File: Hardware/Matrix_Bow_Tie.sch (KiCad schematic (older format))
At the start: 2 parts, among them U1 MAX4466

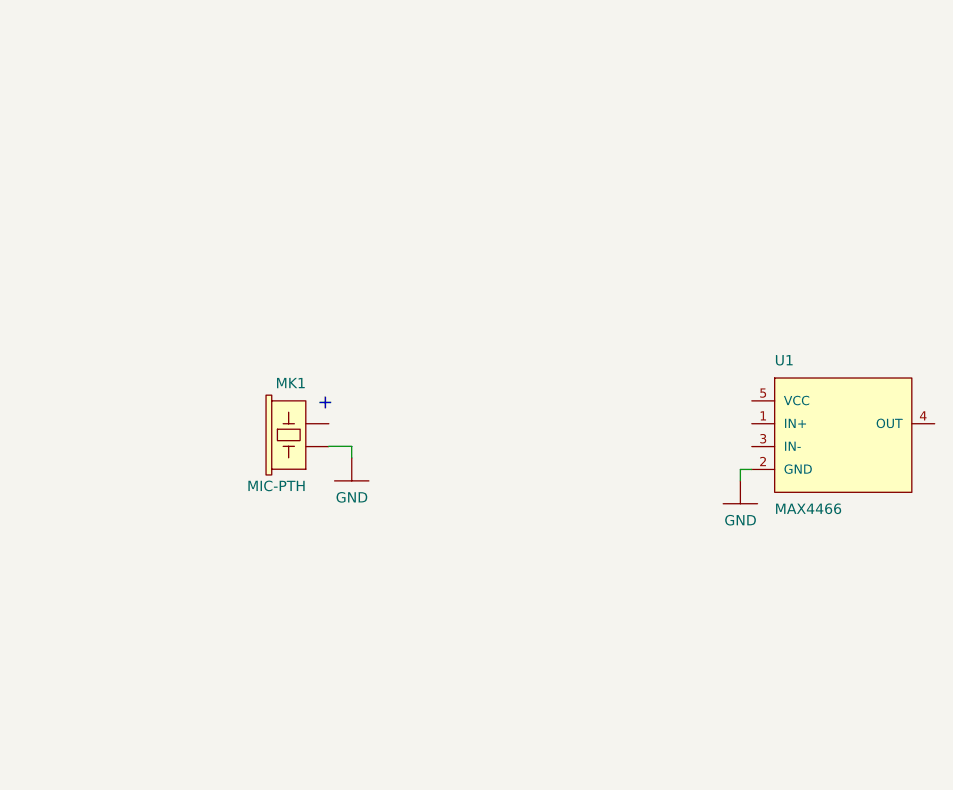
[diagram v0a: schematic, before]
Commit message: Added trimpot footprint and drew mic amp circuit.
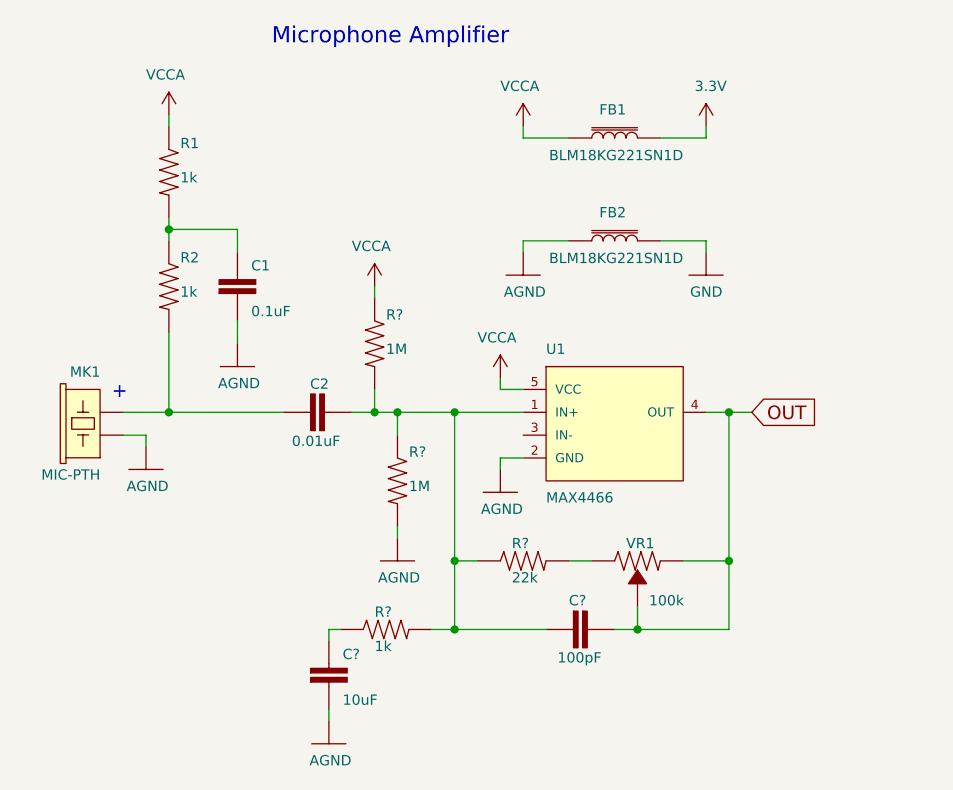
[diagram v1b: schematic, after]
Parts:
- added C1: 0.1uF, 0603, symbol 0.1UF-0603-25V-_+80_-20%_
- added C2: 0.01uF, 0603, symbol 0.1UF-0603-25V-_+80_-20%_
- added C?: 10uF, 0805, symbol 10UF-0805-10V-10%
- added C?: 100pF, 0603, symbol 100PF-0603-50V-5%
- added FB1, FB2: BLM18KG221SN1D, 0603, symbol FERRITE_BEAD-0603
- added R1, R2, R?: 1k, 0603, symbol 1KOHM-0603-1_10W-1%
- added R? (x2): 1M, 0603, symbol 1MOHM-0603-1_4W-5%
- added R?: 22k, 0603, symbol 22KOHM-0603-1_10W-1%
- added VR1: 100k, TC33X, symbol TRIMPOT-TC33X-2
- MK1: footprint Silicon-Custom:MICROPHONE-PTH-9.7MM -> MICROPHONE-PTH-9.7MM
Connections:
- net labels added: 3.3V, AGND, OUT, VCCA
- wire segments 4 -> 38
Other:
- note added: "Microphone Amplifier"
- moved on the sheet: U1

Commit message: Parts mostly laid out
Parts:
- added C5: 0.1uF, Capacitors:0603, symbol 0.1UF-0603-25V-_+80_-20%_
- added D1, D10, D11, D12, D13, D14, D15, D16, D17, D18, D19, D2, D20, D21, D22, D23, D24, D25, D26, D27, D28, D29, D3, D30, D31, D32, D33, D34, D35, D36, D37, D38, D39, D4, D40, D5, D6, D7, D8, D9: Yellow, LED:LED-0603, symbol LED0603
- added H1, H2: STAND-OFF, STAND-OFF, symbol STAND-OFF
- added J1, J2: CONN_12, Matrix_Bot_Tie:1X12_SMD_MALE, symbol CONN_12
- added Q1, Q2, Q3, Q4: TRANS_NPN_DUAL-MBT3904DW1T1, Silicon-Standard:SC70-6, symbol TRANS_NPN_DUAL-MBT3904DW1T1
- added R10, R11, R12, R13, R14, R15, R16, R9: 470, Resistors:0603, symbol 470OHM-0603-1_10W-1%
- added R17, R18, R19, R20, R21: 51, Resistors:0603, symbol 51OHM-0603-1_10W-1%
- added R7, R8: 10K, Resistors:0603, symbol 10KOHM-0603-1_10W-1%
- added S1: MOMENTARY-SWITCH-SPST-2-SMD-4.6X2.8MM, Switches:TACTILE_SWITCH_SMD_4.6X2.8MM, symbol MOMENTARY-SWITCH-SPST-2-SMD-4.6X2.8MM
- added U2: 74HC4051-SOIC16, Matrix_Bot_Tie:SOIC-16, symbol 74HC4051-SOIC16
- C1, C2: footprint 0603 -> Capacitors:0603
- C3: renamed from C?; footprint 0805 -> Capacitors:0805
- C4: renamed from C?; footprint 0603 -> Capacitors:0603
- FB1, FB2: footprint 0603 -> Coils:0603
- MK1: footprint MICROPHONE-PTH-9.7MM -> Silicon-Custom:MICROPHONE-PTH-9.7MM
- R1, R2: footprint 0603 -> Resistors:0603
- R3, R4, R5, R6: renamed from R?; footprint 0603 -> Resistors:0603
- VR1: footprint TC33X -> Matrix_Bot_Tie:TC33X
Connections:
- net 3.3V: now also C5.1, J2.12, R7.1, U2.16 (VCC)
- net GND: now also C5.2, J2.11, Q1.1 (E), Q1.4 (E), Q2.1 (E), Q2.4 (E), Q3.1 (E), Q3.4 (E), Q4.1 (E), Q4.4 (E), R8.2, S1.3, S1.4, U2.7 (VEE), U2.8 (GND)
- net OUT: now also J2.6
- net at C2.2, R3.2, R5.1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: no longer C4.2, R4.2, R6.1
- net at U1.3 (IN-): now also C4.2, R4.2, R6.1
- new net: J2.1, R7.2, S1.1, S1.2
- new net: R13.1, U2.1 (Y4)
- new net: R12.1, U2.12 (Y3)
- new net: R9.1, U2.13 (Y0)
- new net: R10.1, U2.14 (Y1)
- new net: R11.1, U2.15 (Y2)
- new net: R15.1, U2.2 (Y6)
- new net: R16.1, U2.4 (Y7)
- new net: R14.1, U2.5 (Y5)
- new net: Q1.5 (B), R9.2
- new net: Q1.2 (B), R10.2
- new net: Q2.5 (B), R11.2
- new net: Q2.2 (B), R12.2
- new net: Q3.5 (B), R13.2
- new net: Q3.2 (B), R14.2
- new net: Q4.5 (B), R15.2
- new net: Q4.2 (B), R16.2
- new net: D1.C, D2.C, D3.C, D4.C, D5.C, Q1.3 (C)
- new net: D10.C, D6.C, D7.C, D8.C, D9.C, Q1.6 (C)
- new net: D11.C, D12.C, D13.C, D14.C, D15.C, Q2.3 (C)
- new net: D16.C, D17.C, D18.C, D19.C, D20.C, Q2.6 (C)
- new net: D21.C, D22.C, D23.C, D24.C, D25.C, Q3.3 (C)
- new net: D26.C, D27.C, D28.C, D29.C, D30.C, Q3.6 (C)
- new net: D31.C, D32.C, D33.C, D34.C, D35.C, Q4.3 (C)
- new net: D36.C, D37.C, D38.C, D39.C, D40.C, Q4.6 (C)
- new net: D10.A, D15.A, D20.A, D25.A, D30.A, D35.A, D40.A, D5.A, R21.2
- new net: D14.A, D19.A, D24.A, D29.A, D34.A, D39.A, D4.A, D9.A, R20.2
- new net: D13.A, D18.A, D23.A, D28.A, D3.A, D33.A, D38.A, D8.A, R19.2
- new net: D12.A, D17.A, D2.A, D22.A, D27.A, D32.A, D37.A, D7.A, R18.2
- new net: D1.A, D11.A, D16.A, D21.A, D26.A, D31.A, D36.A, D6.A, R17.2
- new net E: J2.2, R8.1, U2.6 (~E~)
- new net R0: J1.8, R17.1
- new net R1: J1.7, R18.1
- new net R2: J2.9, R19.1
- new net R3: J2.8, R20.1
- new net R4: J2.7, R21.1
- new net S0: J2.5, U2.11 (S0)
- new net S1: J2.4, U2.10 (S1)
- new net S2: J2.3, U2.9 (S2)
- new net Z: J2.10, U2.3 (Z)
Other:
- note added: "/RST"
- note added: "A0"
- note added: "A1"
- note added: "A2"
- note added: "A3"
- note added: "A4"
- note added: "A5"
- note added: "D0"
- note added: "D1"
- note added: "D12"
- note added: "D14"
- note added: "D15"
- note added: "D16"
- note added: "D2"
- note added: "D3"
- note added: "D4"
- note added: "D5"
- note added: "D6"
- note added: "D8"
- note added: "D9"
- note added: "GND"
- note added: "L+"
- note added: "LED Array"
- note added: "Qduino Mini Connector"
- note added: "VCC"
- note added: "Vbus"

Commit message: Layout complete. Gerbers ran.
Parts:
- added LOGO1: OSHW-LOGOS, OSHW-LOGO-S, symbol OSHW-LOGOS
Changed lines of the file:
@@
 Wire Wire Line
 	10000 5750 10000 4550
+$Comp
+L OSHW-LOGOS LOGO1
+U 1 1 59B5C1C7
+P 6300 7300
+F 0 "LOGO1" H 6300 7550 45  0001 C CNN
+F 1 "OSHW-LOGOS" H 6300 6900 45  0001 C CNN
+F 2 "OSHW-LOGO-S" H 6300 7600 20  0001 C CNN
+F 3 "" H 6300 7300 60  0001 C CNN
+F 4 "XXX-00000" H 6300 7650 60  0001 C CNN "Field4"
+	1    6300 7300
+	1    0    0    -1
+$EndComp
 $EndSCHEMATC
